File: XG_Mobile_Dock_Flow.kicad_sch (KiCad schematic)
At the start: 38 parts, among them J1 5-1775443-8, J13 39300240, J14 469911008, J17 8730, J2 20455-040E-76, J3 20455-040E-76, J4 3-2362375-4, J5 USB_C_Receptacle, SW1 SW_Push, U1 DS160PR410RNQR, U2 DS160PR410RNQR

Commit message: added more stuff to the schematics
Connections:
- net GND: now also U1.21 (PWDN1), U1.25 (PWDN2), U1.41 (GND), U2.21 (PWDN1), U2.25 (PWDN2), U2.41 (GND)
- net U1_VREG1: now reaches U1.11 (VREG)
- net U1_VREG0: now reaches U1.18 (VREF)
- net U2_VREG1: now reaches U2.11 (VREG)
- net U2_VREG0: now reaches U2.18 (VREF)
- no-connect marks 12 -> 14

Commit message: fixed Rx
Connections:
- net HSI0N: now also J4.A17; no longer J2.34 (PCIE_RXN0)
- net HSI0P: now also J4.A16; no longer J2.35 (PCIE_RXP0)
- net HSI1N: now also J4.A22; no longer J2.28 (PCIE_RXN1)
- net HSI1P: now also J4.A21; no longer J2.29 (PCIE_RXP1)
- net HSI2N: now also J4.A26; no longer J2.22 (PCIE_RXN2)
- net HSI2P: now also J4.A25; no longer J2.23 (PCIE_RXP2)
- net HSI3N: now also J4.A30; no longer J2.16 (PCIE_RXN3)
- net HSI3P: now also J4.A29; no longer J2.17 (PCIE_RXP3)
- net HSI4N: now also J4.A36; no longer J2.10 (PCIE_RXN4)
- net HSI4P: now also J4.A35; no longer J2.11 (PCIE_RXP4)
- net HSI5N: now also J4.A40; no longer J2.4 (PCIE_RXN5)
- net HSI5P: now also J4.A39; no longer J2.5 (PCIE_RXP5)
- net HSI6N: now also J4.A44; no longer J3.39 (PCIE_RXN6)
- net HSI6P: now also J4.A43; no longer J3.40 (PCIE_RXP6)
- net HSI7N: now also J4.A48; no longer J3.33 (PCIE_RXN7)
- net HSI7P: now also J4.A47; no longer J3.34 (PCIE_RXP7)
- net HSIL0N: now also J2.34 (PCIE_RXN0); no longer J4.A17
- net HSIL0P: now also J2.35 (PCIE_RXP0); no longer J4.A16
- net HSIL1N: now also J2.28 (PCIE_RXN1); no longer J4.A22
- net HSIL1P: now also J2.29 (PCIE_RXP1); no longer J4.A21
- net HSIL2N: now also J2.22 (PCIE_RXN2); no longer J4.A26
- net HSIL2P: now also J2.23 (PCIE_RXP2); no longer J4.A25
- net HSIL3N: now also J2.16 (PCIE_RXN3); no longer J4.A30
- net HSIL3P: now also J2.17 (PCIE_RXP3); no longer J4.A29
- net HSIL4N: now also J2.10 (PCIE_RXN4); no longer J4.A36
- net HSIL4P: now also J2.11 (PCIE_RXP4); no longer J4.A35
- net HSIL5N: now also J2.4 (PCIE_RXN5); no longer J4.A40
- net HSIL5P: now also J2.5 (PCIE_RXP5); no longer J4.A39
- net HSIL6N: now also J3.39 (PCIE_RXN6); no longer J4.A44
- net HSIL6P: now also J3.40 (PCIE_RXP6); no longer J4.A43
- net HSIL7N: now also J3.33 (PCIE_RXN7); no longer J4.A48
- net HSIL7P: now also J3.34 (PCIE_RXP7); no longer J4.A47
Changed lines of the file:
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@@
 		)
 	)
-	(label "HSI2P"
+	(label "HSIL2P"
 		(at 74.93 74.93 0)
 		(effects
@@
 		)
 	)
+	(label "HSI5P"
+		(at 223.52 124.46 0)
+		(effects
+			(font
+				(size 1.27 1.27)
+			)
+			(justify left bottom)
+		)
+	)
 	(label "HSIL5P"
-		(at 223.52 124.46 0)
-		(effects
-			(font
-				(size 1.27 1.27)
-			)
-			(justify left bottom)
-		)
-	)
-	(label "HSI5P"
 		(at 74.93 29.21 0)
 		(effects
@@
 		)
 	)
-	(label "HSIL3P"
+	(label "HSI3P"
 		(at 223.52 99.06 0)
 		(effects
@@
 		)
 	)
-	(label "HSIL0P"
+	(label "HSI0P"
 		(at 223.52 66.04 0)
 		(effects
@@
 		)
 	)
-	(label "HSI0N"
+	(label "HSIL0N"
 		(at 74.93 102.87 0)
 		(effects
@@
 		)
 	)
-	(label "HSI3P"
+	(label "HSIL3P"
 		(at 74.93 59.69 0)
 		(effects
@@
 		)
 	)
-	(label "HSIL4N"
+	(label "HSI4N"
 		(at 223.52 116.84 0)
 		(effects
@@
 		)
 	)
-	(label "HSIL6P"
+	(label "HSI6P"
 		(at 265.43 30.48 0)
 		(effects
@@
 		)
 	)
-	(label "HSI4N"
+	(label "HSIL4N"
 		(at 74.93 41.91 0)
 		(effects
@@
 		)
 	)
+	(label "HSI4P"
+		(at 223.52 114.3 0)
+		(effects
+			(font
+				(size 1.27 1.27)
+			)
+			(justify left bottom)
+		)
+	)
 	(label "HSIL4P"
-		(at 223.52 114.3 0)
-		(effects
-			(font
-				(size 1.27 1.27)
-			)
-			(justify left bottom)
-		)
-	)
-	(label "HSI4P"
 		(at 74.93 44.45 0)
 		(effects
@@
 		)
 	)
-	(label "HSI7N"
+	(label "HSIL7N"
 		(at 40.64 100.33 0)
 		(effects
@@
 		)
 	)
-	(label "HSI5N"
+	(label "HSIL5N"
 		(at 74.93 26.67 0)
 		(effects
@@
 		)
 	)
-	(label "HSIL6N"
+	(label "HSI6N"
 		(at 265.43 33.02 0)
 		(effects
@@
 		)
 	)
-	(label "HSIL7P"
+	(label "HSI7P"
 		(at 265.43 40.64 0)
 		(effects
@@
 		)
 	)
-	(label "HSIL0N"
+	(label "HSI0N"
 		(at 223.52 68.58 0)
 		(effects
@@
 		)
 	)
-	(label "HSIL5N"
+	(label "HSI5N"
 		(at 223.52 127 0)
 		(effects
@@
 		)
 	)
-	(label "HSI1N"
+	(label "HSIL1N"
 		(at 74.93 87.63 0)
 		(effects
@@
 		)
 	)
-	(label "HSIL1N"
+	(label "HSI1N"
 		(at 223.52 81.28 0)
 		(effects
@@
 		)
 	)
-	(label "HSIL1P"
+	(label "HSI1P"
 		(at 223.52 78.74 0)
 		(effects
@@
 		)
 	)
-	(label "HSI6P"
+	(label "HSIL6P"
 		(at 40.64 118.11 0)
 		(effects
@@
 		)
 	)
-	(label "HSI2N"
+	(label "HSIL2N"
 		(at 74.93 72.39 0)
 		(effects
@@
 		)
 	)
-	(label "HSI6N"
+	(label "HSIL6N"
 		(at 40.64 115.57 0)
 		(effects
@@
 		)
 	)
-	(label "HSI3N"
+	(label "HSIL3N"
 		(at 74.93 57.15 0)
 		(effects
@@
 		)
 	)
-	(label "HSIL2N"
+	(label "HSI2N"
 		(at 223.52 91.44 0)
 		(effects
@@
 		)
 	)
-	(label "HSIL2P"
+	(label "HSI2P"
 		(at 223.52 88.9 0)
 		(effects
@@
 		)
 	)
-	(label "HSI0P"
+	(label "HSIL0P"
 		(at 74.93 105.41 0)
 		(effects
@@
 		)
 	)
-	(label "HSIL7N"
+	(label "HSI7N"
 		(at 265.43 43.18 0)
 		(effects
@@
 		)
 	)
-	(label "HSI7P"
+	(label "HSIL7P"
 		(at 40.64 102.87 0)
 		(effects
@@
 		)
 	)
-	(label "HSI1P"
+	(label "HSIL1P"
 		(at 74.93 90.17 0)
 		(effects
@@
 		)
 	)
-	(label "HSIL3N"
+	(label "HSI3N"
 		(at 223.52 101.6 0)
 		(effects

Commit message: fixed issues and almost final implementation
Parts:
- added C48, C49, C50, C51: 0.1μF, Capacitor_SMD:C_0402_1005Metric, symbol Device:C
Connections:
- net GND: now also C48.2, C49.2, C50.2, C51.2
- net U1_VREG0: now also C50.1
- net U1_VREG1: now also C51.1
- net U2_VREG0: now also C48.1
- net U2_VREG1: now also C49.1

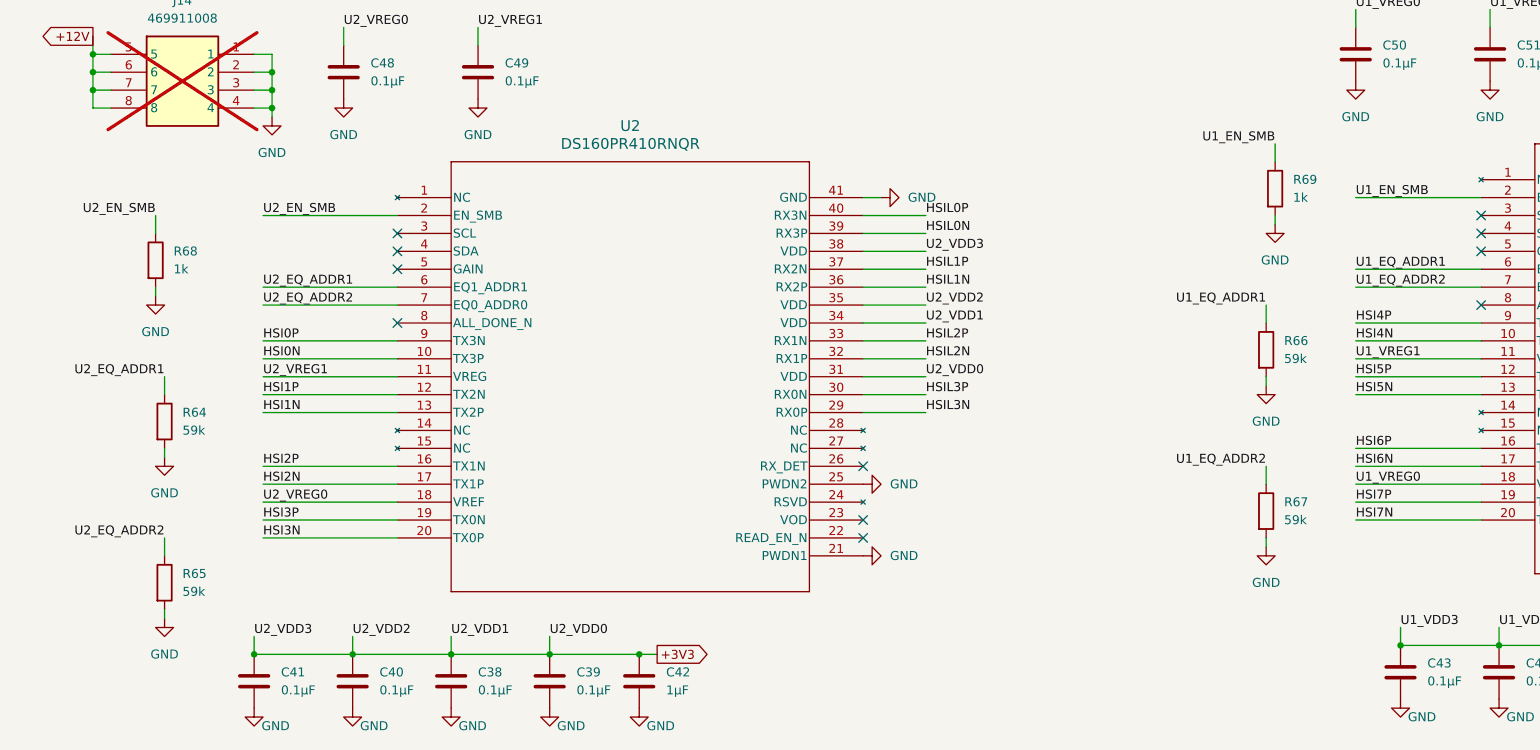
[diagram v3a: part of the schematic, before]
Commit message: added missing ac decoupler caps
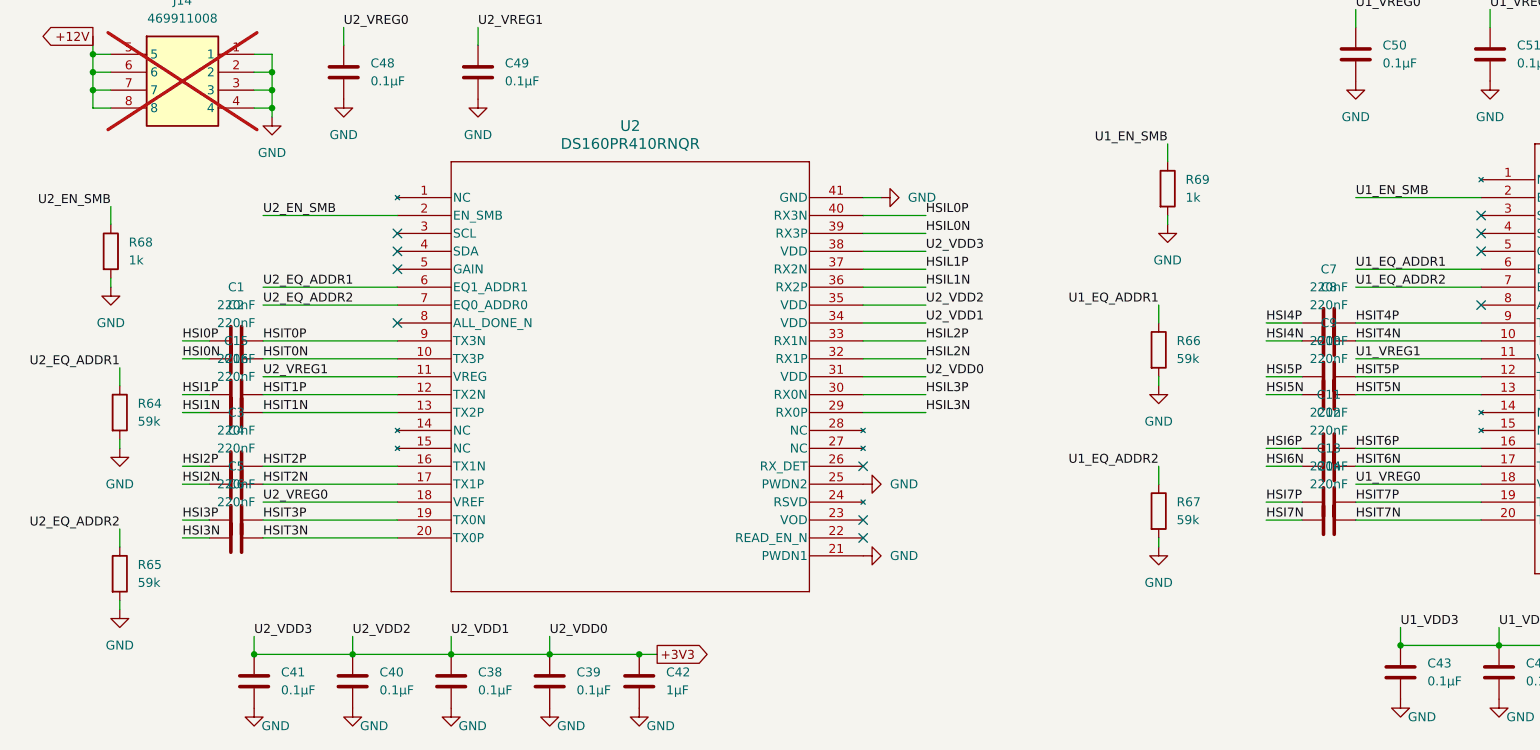
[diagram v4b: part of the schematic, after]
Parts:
- added C1, C10, C11, C12, C13, C14, C15, C16, C2, C3, C4, C5, C6, C7, C8, C9: 220nF, Capacitor_SMD:C_0201_0603Metric, symbol Device:C
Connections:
- net HSI0N: now also C2.2; no longer U2.10 (TX3P)
- net HSI0P: now also C1.2; no longer U2.9 (TX3N)
- net HSI1N: now also C16.2; no longer U2.13 (TX2P)
- net HSI1P: now also C15.2; no longer U2.12 (TX2N)
- net HSI2N: now also C4.2; no longer U2.17 (TX1P)
- net HSI2P: now also C3.2; no longer U2.16 (TX1N)
- net HSI3N: now also C6.2; no longer U2.20 (TX0P)
- net HSI3P: now also C5.2; no longer U2.19 (TX0N)
- net HSI4N: now also C8.2; no longer U1.10 (TX3P)
- net HSI4P: now also C7.2; no longer U1.9 (TX3N)
- net HSI5N: now also C10.2; no longer U1.13 (TX2P)
- net HSI5P: now also C9.2; no longer U1.12 (TX2N)
- net HSI6N: now also C12.2; no longer U1.17 (TX1P)
- net HSI6P: now also C11.2; no longer U1.16 (TX1N)
- net HSI7N: now also C14.2; no longer U1.20 (TX0P)
- net HSI7P: now also C13.2; no longer U1.19 (TX0N)
- new net HSIT0N: C2.1, U2.10 (TX3P)
- new net HSIT0P: C1.1, U2.9 (TX3N)
- new net HSIT1N: C16.1, U2.13 (TX2P)
- new net HSIT1P: C15.1, U2.12 (TX2N)
- new net HSIT2N: C4.1, U2.17 (TX1P)
- new net HSIT2P: C3.1, U2.16 (TX1N)
- new net HSIT3N: C6.1, U2.20 (TX0P)
- new net HSIT3P: C5.1, U2.19 (TX0N)
- new net HSIT4N: C8.1, U1.10 (TX3P)
- new net HSIT4P: C7.1, U1.9 (TX3N)
- new net HSIT5N: C10.1, U1.13 (TX2P)
- new net HSIT5P: C9.1, U1.12 (TX2N)
- new net HSIT6N: C12.1, U1.17 (TX1P)
- new net HSIT6P: C11.1, U1.16 (TX1N)
- new net HSIT7N: C14.1, U1.20 (TX0P)
- new net HSIT7P: C13.1, U1.19 (TX0N)
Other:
- moved on the sheet: R64, R65, R66, R67, R68, R69
